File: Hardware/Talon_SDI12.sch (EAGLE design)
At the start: 88 parts, among them J1 CONN_TALON_REMOTE, J2 CONN_SDI-12_LOGGERM8_TE_BOARD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, J3 CONN_SDI-12_LOGGERM8_TE_BOARD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, J4 CONN_SDI-12_LOGGERM8_TE_BOARD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, J5 CONN_APOGEE_LOGGER, Q1 AO3419, Q2 2N7002, Q3 AO3419, Q4 2N7002, Q5 AO3419, Q6 2N7002, Q7 AO3419, Q8 2N7002, U1 SN74LVC1G00SC70, U10 SN74LVC1G3157SC70, U11 SN74LVC1G3157SC70, U12 SN74LVC1G3157SC70, U13 SN74LVC1G3157SC70, U14 LM2621, U15 MCP3221, U16 LMR62014SOT23, U17 TXS0102DCU, U18 FDC6330L, U2 SN74LVC2G241DCU, U26 MCP23018QFN, U28 74HC4852, U29 SN74AUP1T157DCK, U3 MAX9034TSSOP, U30 MCP3421A3, U31 PCA9536DFN, U4 INA4180A2, U5 CD4044, U6 SN74HC04, U7 SN74AC08, U8 SIP32431TDFN, U9 SN74LVC1G17DCK

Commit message: Layout and cleanup done, review needed
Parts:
- removed R31: 40.2k, bschulz_passives:R-EU_115KR0603
- removed R32: 13.3k, bschulz_passives:R-EU_13.3KR0603
- removed U26: MCP23018QFN, bschulz:MCP23018QFN
- removed U28: 74HC4852, bschulz:74HC4852
- removed U29: SN74AUP1T157DCK, bschulz:SN74AUP1T157DCK
- removed U30: MCP3421A3, bschulz:MCP3421A3
- removed U31: PCA9536DFN, bschulz:PCA9536DFN
- added R29: (no value), bschulz_passives:R-EU_R0603
- added R30: 100k, bschulz_passives:R-EU_100KR0402
- added U19, U20: SN74LVC1G3157SC70, bschulz:SN74LVC1G3157SC70
- added U21: SN74LVC1G00SC70, bschulz:SN74LVC1G00SC70
- added U22: SN74LVC2G241DCU, bschulz:SN74LVC2G241DCU
- added U23: SN74LVC1G17DCK, bschulz:SN74LVC1G17DCK
- C1: value 0.1uF -> 1uF; device bschulz_passives:C-EU0.1UFC0603 -> bschulz_passives:C-EU1UFC0603
- C10, C12, C16: device bschulz_passives:C-EU0.1UFC0603 -> bschulz_passives:C-EU0.1UFC0402
- C11: value 4.7uF -> 0.1uF; device bschulz_passives:C-EU4.7UFC0805 -> bschulz_passives:C-EU0.1UFC0402
- C13: value 10uF -> 0.1uF; device bschulz_passives:C-EU10UFC0805 -> bschulz_passives:C-EU0.1UFC0402
- C14: DIGIKEY 587-2985-1-ND -> (none); MF Taiyo Yuden -> (none); MPN TMK212BBJ106KG-T -> (none)
- C15: value 220pF -> 10uF; device bschulz_passives:C-EU220PFC0603 -> bschulz_passives:C-EU10UFC0805
- C2: value 22uF -> 0.1uF; device bschulz_passives:C-EU22UFC0805 -> bschulz_passives:C-EU0.1UFC0402
- C3: value 0.1uF -> 22uF; device bschulz_passives:C-EU0.1UFC0603 -> bschulz_passives:C-EU22UFC0805
- C4: value (none) -> 0.1uF; device bschulz_passives:C-EUC0603 -> bschulz_passives:C-EU0.1UFC0402
- C5: value 68uF -> 4.7uF; device bschulz_passives:CTANT_EU2917 -> bschulz_passives:C-EU4.7UFC0805
- C6: value 0.1uF -> 220pF; device bschulz_passives:C-EU0.1UFC0603 -> bschulz_passives:C-EU220PFC0603
- C7: value 1uF -> (none); device bschulz_passives:C-EU1UFC0603 -> bschulz_passives:C-EUC0603
- C8: value 0.1uF -> 10uF; device bschulz_passives:C-EU0.1UFC0603 -> bschulz_passives:C-EU10UFC0805; DIGIKEY (none) -> 587-2985-1-ND; MF (none) -> Taiyo Yuden; MPN (none) -> TMK212BBJ106KG-T
- C9: value 10uF -> 68uF; device bschulz_passives:C-EU10UFC0805 -> bschulz_passives:CTANT_EU2917
- J1: value CONN_TALON_REMOTE -> CONN_APOGEE_LOGGER; device GEMS_Plugs:CONN_TALON_REMOTE -> GEMS_Plugs:CONN_APOGEE_LOGGER
- J2: value CONN_SDI-12_LOGGERM8_TE_BOARDLOCK -> CONN_TALON_REMOTE; device GEMS_Plugs:CONN_SDI-12_LOGGERM8_TE_BOARDLOCK -> GEMS_Plugs:CONN_TALON_REMOTE
- J5: value CONN_APOGEE_LOGGER -> CONN_SDI-12_LOGGERM8_TE_BOARDLOCK; device GEMS_Plugs:CONN_APOGEE_LOGGER -> GEMS_Plugs:CONN_SDI-12_LOGGERM8_TE_BOARDLOCK
- Q1, Q3: value AO3419 -> 2N7002; device bschulz:MOSFET-PCH-AO3419 -> bschulz:MOSFET-NCH-2N7002P
- Q6, Q8: value 2N7002 -> AO3419; device bschulz:MOSFET-NCH-2N7002P -> bschulz:MOSFET-PCH-AO3419
- R1, R11, R3, R4: device bschulz_passives:R-EU_10KR0603 -> bschulz_passives:R-EU_10KR0402
- R10: value 82m -> 100k; device bschulz_passives:R-EU_R0603 -> bschulz_passives:R-EU_100KR0402
- R12: value 82m -> 1M; device bschulz_passives:R-EU_R0603 -> bschulz_passives:R-EU_1MR0402
- R13: value 100k -> 470k; device bschulz_passives:R-EU_100KR0603 -> bschulz_passives:R-EU_470KR0603
- R2: value 82m -> 10k; device bschulz_passives:R-EU_R0603 -> bschulz_passives:R-EU_10KR0402
- R22: value (none) -> 40.2k; device bschulz_passives:R-EU_R0603 -> bschulz_passives:R-EU_115KR0603
- R23: value (none) -> 13.3k; device bschulz_passives:R-EU_R0603 -> bschulz_passives:R-EU_13.3KR0603
- R24: value 470k -> 115k; device bschulz_passives:R-EU_470KR0603 -> bschulz_passives:R-EU_115KR0603
- R25: value 115k -> 13.3k; device bschulz_passives:R-EU_115KR0603 -> bschulz_passives:R-EU_13.3KR0603
- R26: value 13.3k -> 10k; device bschulz_passives:R-EU_13.3KR0603 -> bschulz_passives:R-EU_10KR0402
- R27: value 100k -> 10k; device bschulz_passives:R-EU_100KR0603 -> bschulz_passives:R-EU_10KR0402
- R28: value 100k -> (none); device bschulz_passives:R-EU_100KR0603 -> bschulz_passives:R-EU_R0603
- R5: value 1M -> 82m; device bschulz_passives:R-EU_1MR0603 -> bschulz_passives:R-EU_R0603
- R6, R8: value 10k -> 82m; device bschulz_passives:R-EU_10KR0603 -> bschulz_passives:R-EU_R0603
- R9: value 10k -> 100k; device bschulz_passives:R-EU_10KR0603 -> bschulz_passives:R-EU_100KR0402
- U1: value SN74LVC1G00SC70 -> SN74HC04; device bschulz:SN74LVC1G00SC70 -> bschulz:SN74HC04
- U10: value SN74LVC1G3157SC70 -> FXMAR2102UMLP; device bschulz:SN74LVC1G3157SC70 -> bschulz:FXMAR2102UMLP
- U11: value SN74LVC1G3157SC70 -> 74HC4852; device bschulz:SN74LVC1G3157SC70 -> bschulz:74HC4852
- U12: value SN74LVC1G3157SC70 -> SN74AUP1T157DCK; device bschulz:SN74LVC1G3157SC70 -> bschulz:SN74AUP1T157DCK
- U13: value SN74LVC1G3157SC70 -> MCP3221; device bschulz:SN74LVC1G3157SC70 -> bschulz:MCP3221
- U14: value LM2621 -> MCP23018QFN; device bschulz:LM2621 -> bschulz:MCP23018QFN
- U15: value MCP3221 -> PCA9536DFN; device bschulz:MCP3221 -> bschulz:PCA9536DFN
- U16: value LMR62014SOT23 -> MCP3421A3; device bschulz:LMR62014SOT23 -> bschulz:MCP3421A3
- U17: value TXS0102DCU -> SN74LVC1G3157SC70; device bschulz:TXS0102DCU -> bschulz:SN74LVC1G3157SC70
- U18: value FDC6330L -> SN74LVC1G3157SC70; device bschulz:FDC6330L -> bschulz:SN74LVC1G3157SC70
- U2: value SN74LVC2G241DCU -> CD4044; device bschulz:SN74LVC2G241DCU -> bschulz:CD4044
- U3: value MAX9034TSSOP -> SIP32431TDFN; device bschulz:MAX9034TSSOP -> bschulz:SIP32431TDFN
- U5: value CD4044 -> MAX9034TSSOP; device bschulz:CD4044 -> bschulz:MAX9034TSSOP
- U6: value SN74HC04 -> SI1869; device bschulz:SN74HC04 -> bschulz:SI1869
- U8: value SIP32431TDFN -> LM2621; device bschulz:SIP32431TDFN -> bschulz:LM2621
- U9: value SN74LVC1G17DCK -> LMR62014SOT23; device bschulz:SN74LVC1G17DCK -> bschulz:LMR62014SOT23
- renumbered D4 to D3, L3 to L2
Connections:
- net !FAULT1: now also U1.A4, U14.GPB0, U2.Q2; no longer U26.GPB0, U5.Q2, U6.A4
- net !FAULT2: now also U1.A2, U14.GPB1, U2.Q1; no longer U26.GPB1, U5.Q1, U6.A2
- net !FAULT3: now also U1.A3, U14.GPB2, U2.Q3; no longer U26.GPB2, U5.Q3, U6.A3
- net !FAULT4: now also U1.A1, U14.GPB3, U2.Q4; no longer U26.GPB3, U5.Q4, U6.A1
- net !RX: now also U22.1Y, U23.A; no longer U2.1Y, U9.A
- net 12V: now also C7.1, C9.+, Q6.S, Q8.S, R10.2, R2.2, R24.2, R3.2, R4.2, U6.VIN; no longer C4.1, C5.+, Q1.S, Q3.S, R11.2, R25.2, R27.2, R6.2, R9.2, U18.VIN
- net 3V3: now also C14.1, C16.1, C4.1, C5.1, J2.3V3, R12.2, R13.2, R26.2, R27.2, R28.2, U1.A5, U1.A6, U10.EN, U10.VA, U11.VCC, U12.VCC, U14.!RESET, U15.VCC, U16.VDD, U2.EN, U2.VCC, U21.VCC, U23.VCC, U3.VIN, U8.BOOT, U8.EN, U8.VDD, U9.!SHDN, U9.VIN; no longer C11.1, C13.1, C2.1, C7.1, J1.3V3, R22.2, R24.2, R3.2, R4.2, R5.2, U14.BOOT, U14.EN, U16.!SHDN, U16.VIN, U17.EN, U17.VA, U26.!RESET, U26.VDD, U28.VCC, U29.VCC, U30.VDD, U31.VCC, U5.EN, U5.VCC, U6.A5, U6.A6, U6.VCC, U8.VIN, U9.VCC
- net 3V3_SENSE: now also C2.1, R11.2, U3.VOUT, U5.VDD; no longer C8.1, R8.2, U3.VDD, U8.VOUT
- net 5V: now also C11.1, C13.1, C8.1, R22.2, U10.VB, U13.VDD, U17.VCC, U18.VCC, U19.VCC, U20.VCC, U22.VCC; no longer C14.1, C16.1, C9.1, R31.2, U10.VCC, U11.VCC, U12.VCC, U13.VCC, U15.VDD, U17.VB, U2.VCC
- net DATA: now also U17.B2, U18.B2, U19.B2, U20.B2, U22.1A, U22.2Y; no longer U10.B2, U11.B2, U12.B2, U13.B2, U2.1A, U2.2Y
- net DATA_EN1: now also U14.GPA4, U17.S; no longer U10.S, U26.GPA4
- net DATA_EN2: now also U14.GPA5, U18.S; no longer U11.S, U26.GPA5
- net DATA_EN3: now also U14.GPA6, U19.S; no longer U12.S, U26.GPA6
- net DATA_EN4: now also R30.2, U14.GPA7, U20.S, U6.EN; no longer R28.2, U13.S, U18.EN, U26.GPA7
- net DATA_OUT1: now also J3.DATA, U17.A; no longer J2.DATA, U10.A
- net DATA_OUT2: now also J4.DATA, U18.A; no longer J3.DATA, U11.A
- net DATA_OUT3: now also J5.DATA, U19.A; no longer J4.DATA, U12.A
- net DATA_OUT4: now also J1.3, U20.A; no longer J5.3, U13.A
- net DATA_SENSE4: now also U13.VIN, U20.B1; no longer U13.B1, U15.VIN
- net DIR: now also U14.GPB7, U22.1!OE, U22.2OE; no longer U2.1!OE, U2.2OE, U26.GPB7
- net EN1: now also U14.GPA0, U2.R2; no longer U26.GPA0, U5.R2
- net EN2: now also U14.GPA1, U2.R1; no longer U26.GPA1, U5.R1
- net EN3: now also U14.GPA2, U2.R3; no longer U26.GPA2, U5.R3
- net EN4: now also U14.GPA3, U2.R4; no longer U26.GPA3, U5.R4
- net FAULT1: now also U1.Y4; no longer U6.Y4
- net FAULT2: now also U1.Y2; no longer U6.Y2
- net FAULT3: now also U1.Y3; no longer U6.Y3
- net FAULT4: now also U1.Y1; no longer U6.Y1
- net FOUT: now also U14.GPB6, U21.A; no longer U1.A, U26.GPB6
- net GND: now also C15.2, C3.2, C5.2, C9.-, J1.1, J1.6, J5.GND, Q1.S, Q3.S, R18.1, R20.1, R25.1, R29.1, R30.1, R9.1, U13.VSS, U14.VSS, U15.GND, U16.VIN-, U16.VSS, U18.GND, U19.GND, U20.GND, U21.GND, U22.GND, U23.GND, U6.R2, U8.PGND, U8.SGND; no longer C5.-, C6.2, C7.2, C9.2, J1.GND, J5.1, J5.6, Q6.S, Q8.S, R13.1, R15.1, R17.1, R26.1, R28.1, R32.1, U13.GND, U14.PGND, U14.SGND, U15.VSS, U16.GND, U18.R2, U26.VSS, U28.GND, U29.GND, U30.VIN-, U30.VSS, U31.GND, U6.GND, U8.GND
- net LATCH1: now also U2.S2, U5.OUTA; no longer U3.OUTA, U5.S2
- net LATCH2: now also U2.S1, U5.OUTB; no longer U3.OUTB, U5.S1
- net LATCH3: now also U2.S3, U5.OUTC; no longer U3.OUTC, U5.S3
- net LATCH4: now also U2.S4, U5.OUTD; no longer U3.OUTD, U5.S4
- net MOS_CTRL1: now also Q1.G; no longer Q2.G
- net MOS_CTRL2: now also Q2.G; no longer Q4.G
- net MOS_CTRL3: now also Q3.G; no longer Q6.G
- net MOS_CTRL4: now also Q4.G; no longer Q8.G
- net MUX_EN: now also U11.!E, U15.P3; no longer U28.!E, U31.P3
- net MUX_SEL0: now also U11.S0, U15.P0; no longer U28.S0, U31.P0
- net MUX_SEL1: now also U11.S1, U15.P1; no longer U28.S1, U31.P1
- net MUX_SEL2: now also U12.C, U15.P2; no longer U29.C, U31.P2
- net N$1: now also Q2.D, Q6.G, R2.1; no longer Q3.G, Q4.D, R9.1
- net N$10: now also C6.2, R22.1, R23.2, U9.FB; no longer C15.2, R31.1, R32.2, U16.FB
- net N$11: now also R10.1, U6.R1,C1; no longer R27.1, U18.R1,C1
- net N$14: now also R28.1, R29.2, U14.ADDR; no longer R21.2, R22.1, U26.ADDR
- net N$18: now also U11.2Z, U12.B; no longer U28.2Z, U29.B
- net N$2: now also Q1.D, Q5.G, R1.1; no longer Q1.G, Q2.D, R6.1
- net N$3: now also Q3.D, Q7.G, R3.1; no longer Q5.G, Q6.D, R11.1
- net N$38: now also U11.1Z, U12.A; no longer U28.1Z, U29.A
- net N$4: now also Q4.D, Q8.G, R4.1; no longer Q7.G, Q8.D, R1.1
- net N$5: now also U21.Y, U22.2A; no longer U1.Y, U2.2A
- net N$7: now also C4.2, R13.1, U8.FREQ; no longer C3.2, R24.1, U14.FREQ
- net N$8: now also U8.SW; no longer U14.SW
- net N$9: now also C7.2, R24.1, R25.2, U8.FB; no longer C4.2, R25.1, R26.2, U14.FB
- net POS_DETECT: now also R12.1, U14.GPB4; no longer R5.1, U26.GPB4
- net RX: now also J2.RX, U23.Y; no longer J1.RX, U9.Y
- net SCL: now also J2.SCL, R27.1, U10.A2, U14.SCL, U15.SCL, U16.SCL; no longer J1.SCL, R4.1, U17.A2, U26.SCL, U30.SCL, U31.SCL
- net SCL_HV: now also U10.B2, U13.SCL; no longer U15.SCL, U17.B2
- net SDA: now also J2.SDA, R26.1, U10.A1, U14.SDA, U15.SDA, U16.SDA; no longer J1.SDA, R3.1, U17.A1, U26.SDA, U30.SDA, U31.SDA
- net SDA_HV: now also U10.B1, U13.SDA; no longer U15.SDA, U17.B1
- net SENSE1: now also U11.1Y0, U5.INA-; no longer U28.1Y0, U3.INA-
- net SENSE1+: now also Q5.D, R5.1; no longer Q1.D, R7.1
- net SENSE2: now also U11.1Y1, U5.INB-; no longer U28.1Y1, U3.INB-
- net SENSE2+: now also Q6.D, R6.1; no longer Q3.D, R10.1
- net SENSE3: now also U11.1Y2, U5.INC-; no longer U28.1Y2, U3.INC-
- net SENSE3+: now also Q7.D, R7.1; no longer Q5.D, R12.1
- net SENSE4: now also U11.1Y3, U5.IND-; no longer U28.1Y3, U3.IND-
- net SENSE4+: now also Q8.D, R8.1; no longer Q7.D, R2.1
- net SENSE_EN: now also R9.2, U14.GPB5, U3.EN; no longer R13.2, U26.GPB5, U8.EN
- net SW1: now also U9.SW; no longer U16.SW
- net SWITCHED_SENSE: now also U12.Y, U16.VIN+; no longer U29.Y, U30.VIN+
- net TX: now also J2.TX, U21.B; no longer J1.TX, U1.B
- net VHEATER: now also J1.5, U6.VOUT; no longer J5.5, U18.VOUT
- net VPORT1_OUT: now also J3.12V, R5.2; no longer J2.12V, R7.2
- net VPORT1_OUT_SENSE: now also R18.2, U11.2Y0; no longer R15.2, U28.2Y0
- net VPORT2_OUT: now also J4.12V, R15.1, R6.2; no longer J3.12V, R10.2, R16.1
- net VPORT2_OUT_SENSE: now also R15.2, R19.2, U11.2Y1; no longer R16.2, R17.2, U28.2Y1
- net VPORT3_OUT: now also J5.12V, R16.1, R7.2; no longer J4.12V, R12.2, R18.1
- net VPORT3_OUT_SENSE: now also R16.2, R20.2, U11.2Y2; no longer R18.2, R19.2, U28.2Y2
- net VPORT4_OUT: now also J1.2, R17.1, R8.2; no longer J5.2, R2.2, R20.1
- net VPORT4_OUT_SENSE: now also R17.2, R21.2, U11.2Y3; no longer R20.2, R23.2, U28.2Y3
- net VREF: now also R11.1, U5.INA+, U5.INB+, U5.INC+, U5.IND+; no longer R8.1, U3.INA+, U3.INB+, U3.INC+, U3.IND+

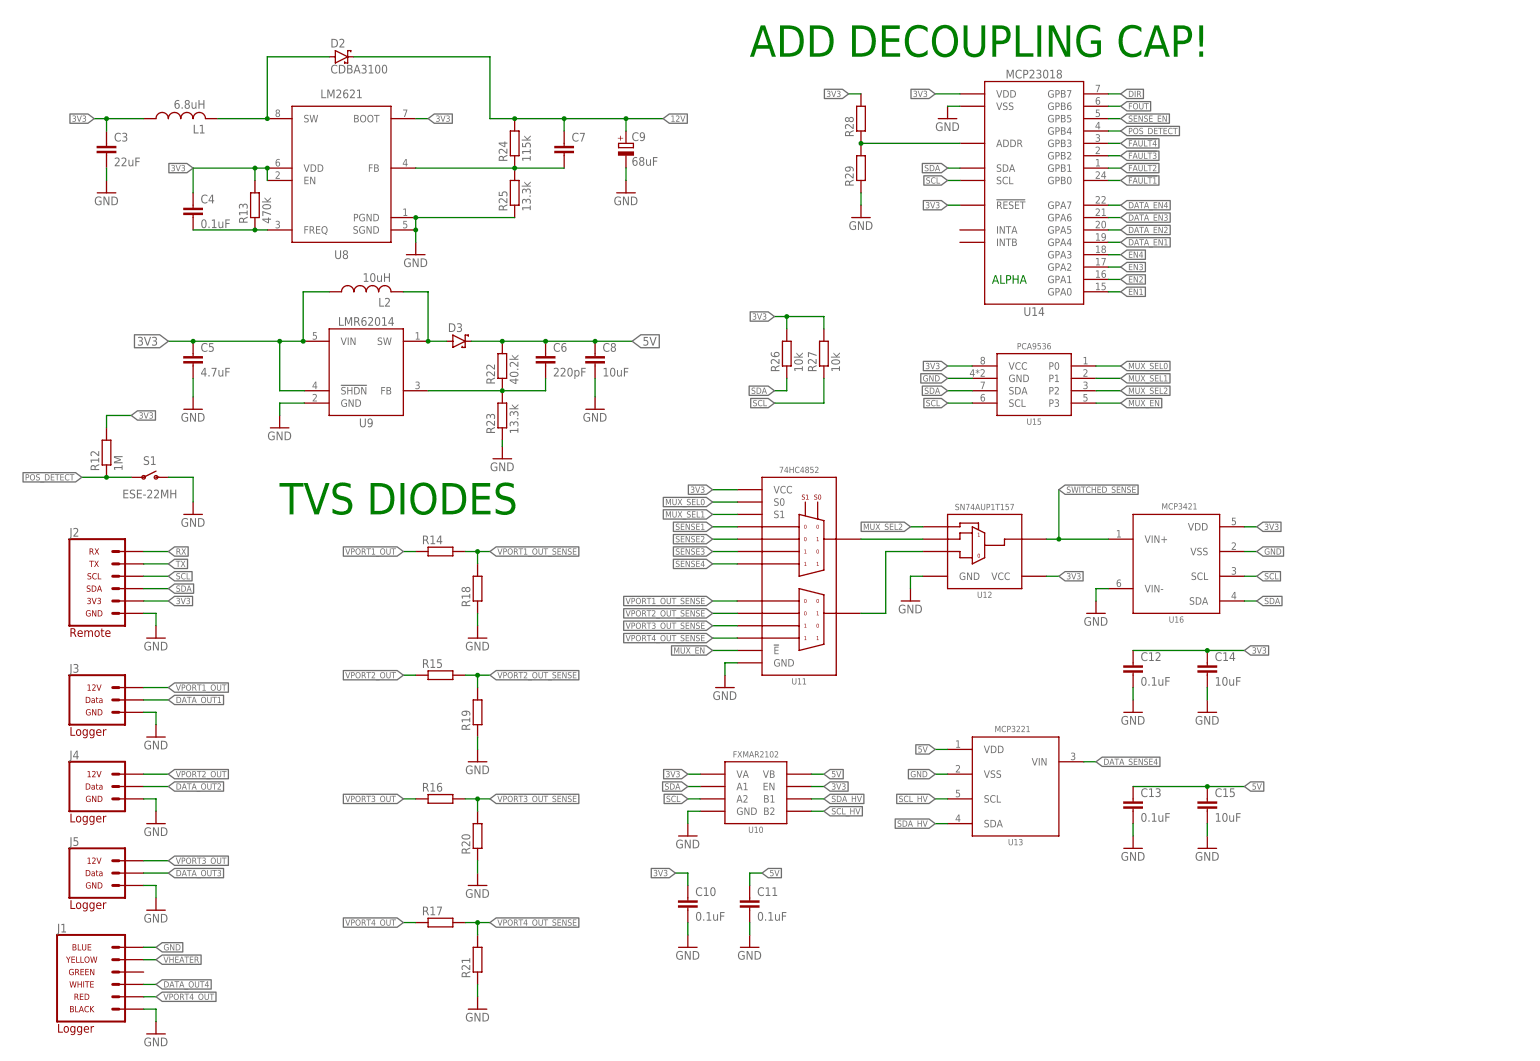
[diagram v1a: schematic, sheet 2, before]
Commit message: Layout, gerbers, and BoM for v0.0 - submitted to fab
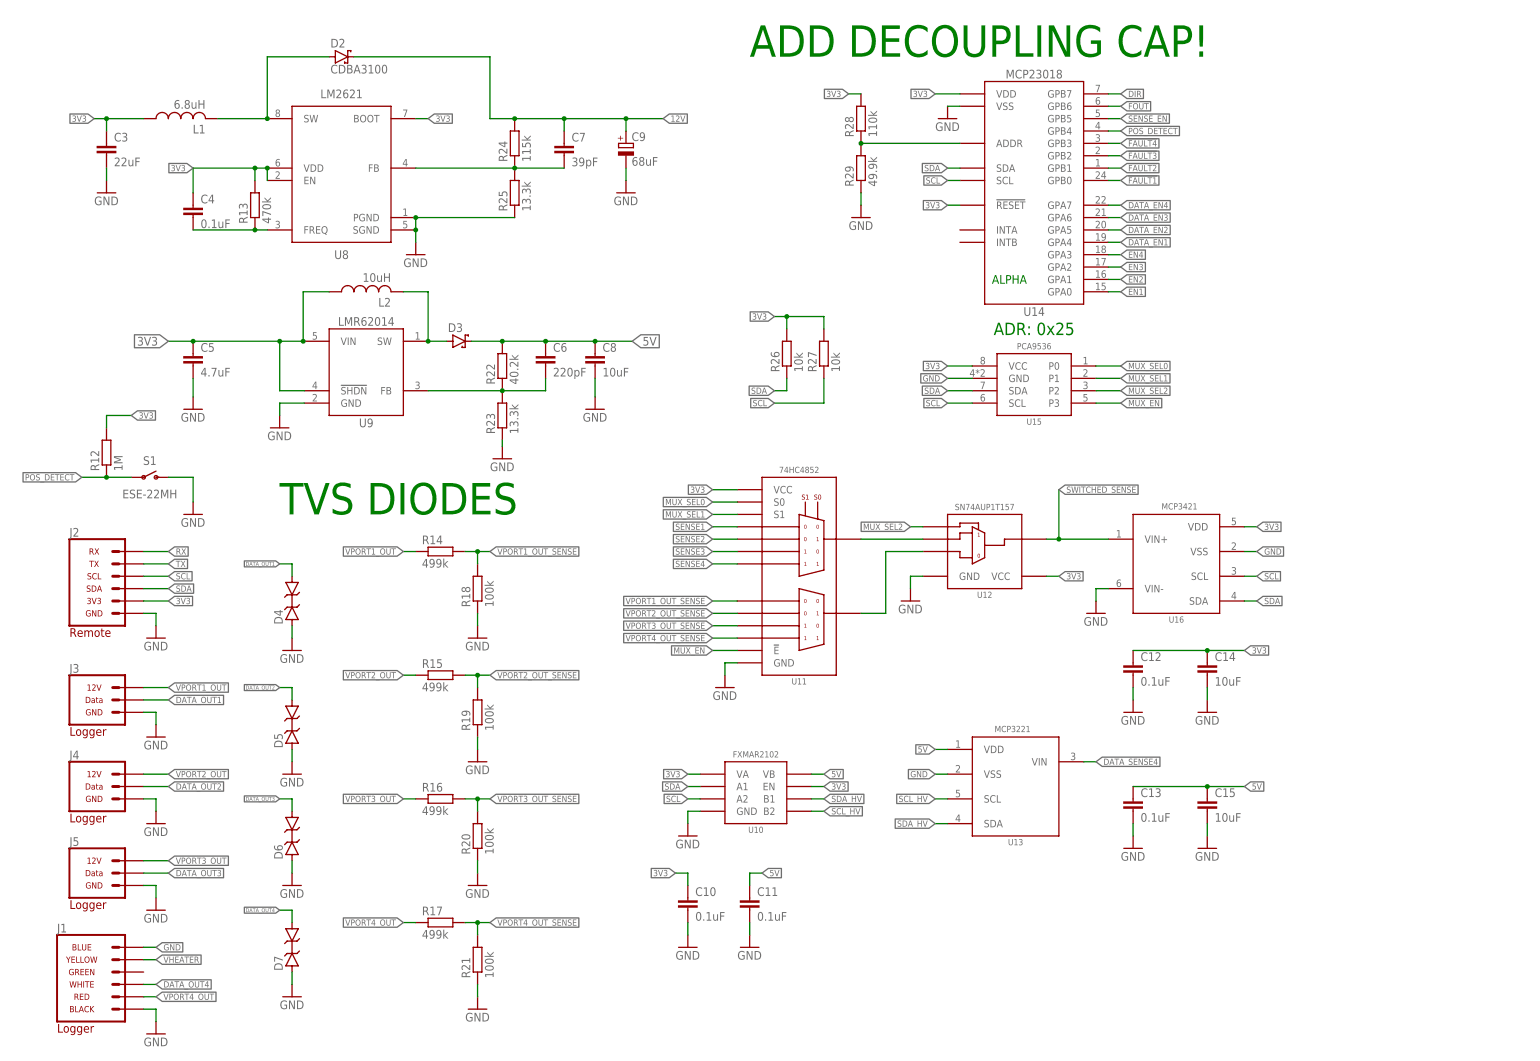
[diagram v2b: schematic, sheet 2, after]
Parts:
- added D4, D5, D6, D7: 6V, bschulz:DIODE_ESD_BI_D5V0L1_0402
- added TP1, TP2, TP3, TP4, TP5, TP6, TP7: TESTPOINTRCU, bschulz:TESTPOINTRCU
- C7: value (none) -> 39pF; device bschulz_passives:C-EUC0603 -> bschulz_passives:C-EU39PFC0402
- C9: DIGIKEY (none) -> 399-3803-1-ND; MF (none) -> Kemet; MPN (none) -> T491D686K020AT
- D2: DIGIKEY (none) -> 641-1747-1-ND; MF (none) -> Comchip; MPN (none) -> CDBA3100-HF
- L1: DIGIKEY (none) -> 732-11744-1-ND; MF (none) -> Wurth; MPN (none) -> 78438357068
- R14, R15, R16, R17: value (none) -> 499k; device bschulz_passives:R-EU_R0603 -> bschulz_passives:R-EU_499KR0603
- R18, R19, R20, R21: value (none) -> 100k; device bschulz_passives:R-EU_R0603 -> bschulz_passives:R-EU_100KR0603
- R22: device bschulz_passives:R-EU_115KR0603 -> bschulz_passives:R-EU_40.2KR0603
- R28: value (none) -> 110k; device bschulz_passives:R-EU_R0603 -> bschulz_passives:R-EU_110KR0603
- R29: value (none) -> 49.9k; device bschulz_passives:R-EU_R0603 -> bschulz_passives:R-EU_49.9KR0603
- R5, R6, R7, R8: device bschulz_passives:R-EU_R0603 -> bschulz_passives:R-EU_0.082R0603
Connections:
- net DATA: now also TP4.P$1
- net DATA_OUT1: now also D4.C
- net DATA_OUT2: now also D5.C
- net DATA_OUT3: now also D6.C
- net DATA_OUT4: now also D7.C
- net DIR: now also TP5.P$1
- net GND: now also D4.A, D5.A, D6.A, D7.A, TP1.P$1
- net RX: now also TP3.P$1
- net SCL: now also TP7.P$1
- net SDA: now also TP6.P$1
- net TX: now also TP2.P$1
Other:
- note added: "ADR: 0x25"

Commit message: V0.1 Updates - Added EEPROM
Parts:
- added U24: 24AA02SOT23, bschulz:24AA02SOT23
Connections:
- net 3V3: now also U24.VCC
- net GND: now also U24.GND, U24.WP
- net SCL: now also U24.SCL
- net SDA: now also U24.SDA
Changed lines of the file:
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@@
 <layer number="128" name="_bValues" color="7" fill="1" visible="no" active="yes"/>
 <layer number="129" name="Mask" color="7" fill="1" visible="no" active="yes"/>
+<layer number="130" name="SMDSTROOK" color="7" fill="1" visible="no" active="yes"/>
 <layer number="131" name="tAdjust" color="7" fill="1" visible="no" active="yes"/>
 <layer number="132" name="bAdjust" color="7" fill="1" visible="no" active="yes"/>
+<layer number="133" name="bottom_silk" color="7" fill="1" visible="no" active="yes"/>
+<layer number="134" name="mbFinish" color="7" fill="1" visible="no" active="no"/>
+<layer number="135" name="mtGlue" color="7" fill="1" visible="no" active="no"/>
+<layer number="136" name="mbGlue" color="7" fill="1" visible="no" active="no"/>
+<layer number="137" name="mtTest" color="7" fill="1" visible="no" active="no"/>
+<layer number="138" name="mbTest" color="7" fill="1" visible="no" active="no"/>
+<layer number="139" name="mtKeepout" color="7" fill="1" visible="no" active="no"/>
+<layer number="140" name="mbKeepout" color="7" fill="1" visible="no" active="no"/>
+<layer number="141" name="mtRestrict" color="7" fill="1" visible="no" active="no"/>
+<layer number="142" name="mbRestrict" color="7" fill="1" visible="no" active="no"/>
+<layer number="143" name="mvRestrict" color="7" fill="1" visible="no" active="no"/>
 <layer number="144" name="Drill_legend" color="7" fill="1" visible="no" active="yes"/>
+<layer number="145" name="mHoles" color="7" fill="1" visible="no" active="no"/>
+<layer number="146" name="mMilling" color="7" fill="1" visible="no" active="no"/>
+<layer number="147" name="mMeasures" color="7" fill="1" visible="no" active="no"/>
+<layer number="148" name="mDocument" color="7" fill="1" visible="no" active="no"/>
+<layer number="149" name="mReference" color="7" fill="1" visible="no" active="no"/>
 <layer number="150" name="Notes" color="7" fill="1" visible="no" active="yes"/>
 <layer number="151" name="HeatSink" color="7" fill="1" visible="no" active="yes"/>
@@
 <layer number="154" name="FabDoc2" color="7" fill="1" visible="no" active="yes"/>
 <layer number="155" name="FabDoc3" color="7" fill="1" visible="no" active="yes"/>
+<layer number="166" name="AntennaArea" color="7" fill="1" visible="no" active="yes"/>
+<layer number="168" name="4mmHeightArea" color="7" fill="1" visible="no" active="yes"/>
+<layer number="191" name="mNets" color="7" fill="1" visible="no" active="no"/>
+<layer number="192" name="mBusses" color="7" fill="1" visible="no" active="no"/>
+<layer number="193" name="mPins" color="7" fill="1" visible="no" active="no"/>
+<layer number="194" name="mSymbols" color="7" fill="1" visible="no" active="no"/>
+<layer number="195" name="mNames" color="7" fill="1" visible="no" active="no"/>
+<layer number="196" name="mValues" color="7" fill="1" visible="no" active="no"/>
 <layer number="199" name="Contour" color="7" fill="1" visible="no" active="yes"/>
 <layer number="200" name="200bmp" color="7" fill="1" visible="no" active="yes"/>
@@
 <part name="D7" library="bschulz" deviceset="DIODE_ESD_BI" device="_0402" technology="_D5V0L1" value="6V"/>
 <part name="GND57" library="supply1" library_urn="urn:adsk.eagle:library:371" deviceset="GND" device=""/>
+<part name="U24" library="bschulz" deviceset="24AA02" device="SOT23"/>
+<part name="GND58" library="supply1" library_urn="urn:adsk.eagle:library:371" deviceset="GND" device=""/>
 </parts>
 <sheets>
@@
 <attribute name="VALUE" x="241.3" y="58.42" size="1.778" layer="96"/>
 </instance>
+<instance part="U24" gate="G$1" x="111.76" y="33.02" smashed="yes">
+<attribute name="DISP" x="111.76" y="42.164" size="1.778" layer="95" ratio="15" align="center"/>
+<attribute name="NAME" x="111.76" y="23.876" size="1.778" layer="95" ratio="15" align="center"/>
+</instance>
+<instance part="GND58" gate="1" x="96.52" y="22.86" smashed="yes">
+<attribute name="VALUE" x="93.98" y="20.32" size="1.778" layer="96"/>
+</instance>
 </instances>
 <busses>
@@
 <junction x="109.22" y="172.72"/>
 <label x="106.68" y="172.72" size="1.27" layer="95" rot="R180" xref="yes"/>
+</segment>
+<segment>
+<pinref part="U24" gate="G$1" pin="VCC"/>
+<wire x1="99.06" y1="38.1" x2="91.44" y2="38.1" width="0.1524" layer="91"/>
+<label x="91.44" y="38.1" size="0.8128" layer="95" rot="R180" xref="yes"/>
 </segment>
 </net>
@@
 <pinref part="GND47" gate="1" pin="GND"/>
 </segment>
+<segment>
+<pinref part="U24" gate="G$1" pin="WP"/>
+<wire x1="124.46" y1="38.1" x2="127" y2="38.1" width="0.1524" layer="91"/>
+<label x="127" y="38.1" size="0.8128" layer="95" xref="yes"/>
+</segment>
+<segment>
+<pinref part="U24" gate="G$1" pin="GND"/>
+<wire x1="99.06" y1="27.94" x2="96.52" y2="27.94" width="0.1524" layer="91"/>
+<wire x1="96.52" y1="27.94" x2="96.52" y2="25.4" width="0.1524" layer="91"/>
+<pinref part="GND58" gate="1" pin="GND"/>
+</segment>
 </net>
 <net name="MOS_CTRL1" class="0">
@@
 </segment>
 </net>
+<net name="SDA" class="0">
+<segment>
+<pinref part="U24" gate="G$1" pin="SDA"/>
+<wire x1="124.46" y1="30.48" x2="127" y2="30.48" width="0.1524" layer="91"/>
+<label x="127" y="30.48" size="0.8128" layer="95" xref="yes"/>
+</segment>
+</net>
+<net name="SCL" class="0">
+<segment>
+<pinref part="U24" gate="G$1" pin="SCL"/>
+<wire x1="124.46" y1="27.94" x2="127" y2="27.94" width="0.1524" layer="91"/>
+<label x="127" y="27.94" size="0.8128" layer="95" xref="yes"/>
+</segment>
+</net>
